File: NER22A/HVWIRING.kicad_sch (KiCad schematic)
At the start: 1 part

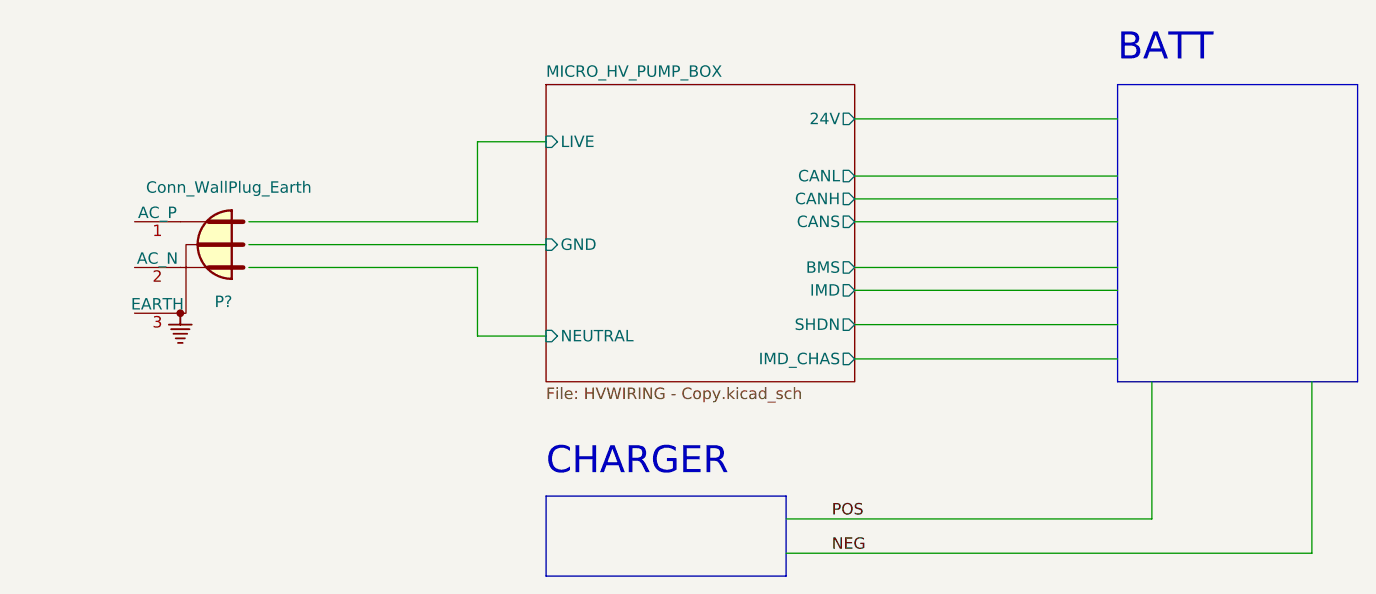
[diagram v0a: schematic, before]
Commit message: Finished wiring diagram
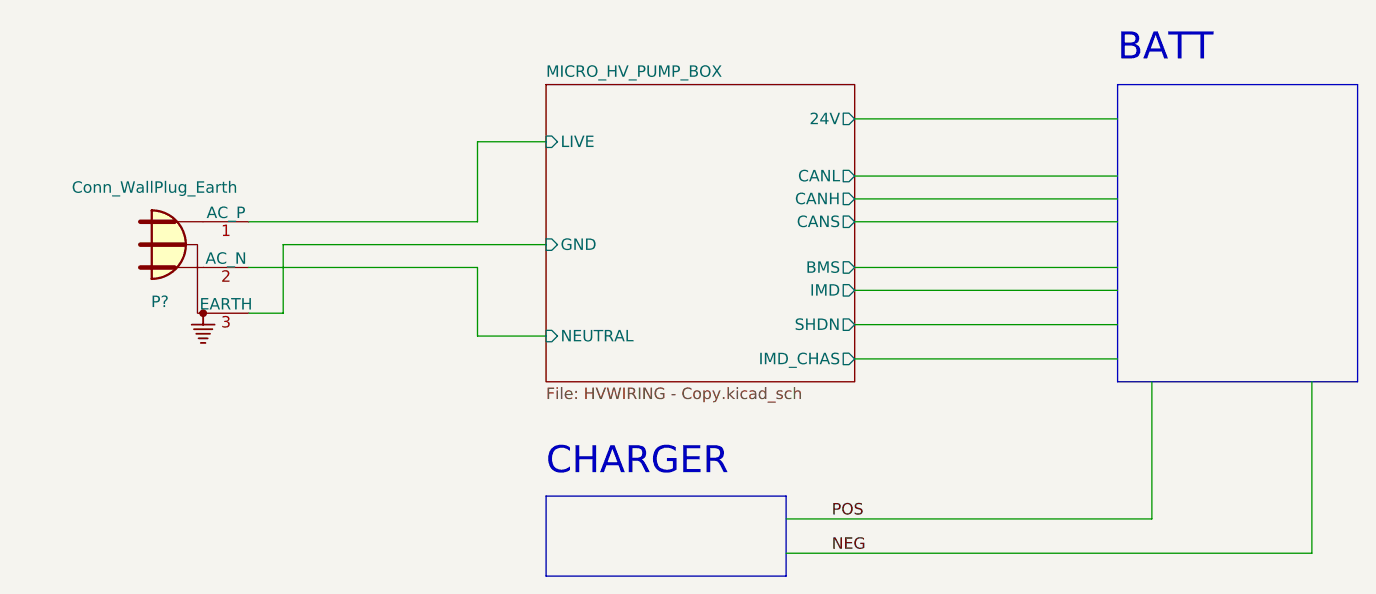
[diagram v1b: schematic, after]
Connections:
- net MICRO_HV_PUMP_BOX/GND: now also P?.3 (EARTH)
- net MICRO_HV_PUMP_BOX/LIVE: now also P?.1 (AC_P)
- net MICRO_HV_PUMP_BOX/NEUTRAL: now also P?.2 (AC_N)
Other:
- moved on the sheet: P?
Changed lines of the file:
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@@
 (kicad_sch (version 20230121) (generator eeschema)
-  (paper "A4")
+  (paper "A")
   (wire (pts (xy 157.48 88.9) (xy 157.48 104.14))
+    (stroke (width 0) (type default))
+  )
+  (wire (pts (xy 57.15 71.12) (xy 82.55 71.12))
     (stroke (width 0) (type default))
   )
@@
     (stroke (width 0) (type default))
   )
+  (wire (pts (xy 60.96 81.28) (xy 57.15 81.28))
+    (stroke (width 0) (type default))
+  )
   (polyline (pts (xy 90.17 101.6) (xy 116.84 101.6))
+    (stroke (width 0) (type default))
+  )
+  (wire (pts (xy 57.15 76.2) (xy 82.55 76.2))
     (stroke (width 0) (type default))
   )
@@
     (stroke (width 0) (type default))
   )
-  (polyline (pts (xy 90.17 101.6) (xy 90.17 110.49))
+  (wire (pts (xy 60.96 73.66) (xy 90.17 73.66))
     (stroke (width 0) (type default))
   )
-  (wire (pts (xy 57.15 73.66) (xy 90.17 73.66))
+  (polyline (pts (xy 90.17 101.6) (xy 90.17 110.49))
     (stroke (width 0) (type default))
   )
@@
     (stroke (width 0) (type default))
   )
-  (wire (pts (xy 116.84 104.14) (xy 157.48 104.14))
+  (wire (pts (xy 60.96 73.66) (xy 60.96 81.28))
     (stroke (width 0) (type default))
   )
-  (wire (pts (xy 57.15 76.2) (xy 82.55 76.2))
+  (wire (pts (xy 116.84 104.14) (xy 157.48 104.14))
     (stroke (width 0) (type default))
   )
@@
   )
   (wire (pts (xy 124.46 82.55) (xy 153.67 82.55))
-    (stroke (width 0) (type default))
-  )
-  (wire (pts (xy 57.15 71.12) (xy 82.55 71.12))
     (stroke (width 0) (type default))
   )
@@
     (effects (font (size 1.27 1.27)) (justify left bottom))
   )
-  (symbol (lib_id "Connector:Conn_WallPlug_Earth") (at 52.07 73.66 0) (mirror y) (unit 1)
+  (symbol (lib_id "Connector:Conn_WallPlug_Earth") (at 49.53 73.66 0) (unit 1)
     (in_bom yes) (on_board yes) (dnp no)
-    (property "Reference" "P?" (at 53.34 80.01 0)
+    (property "Reference" "P?" (at 48.26 80.01 0)
       (effects (font (size 1.27 1.27)) (justify right))
     )
-    (property "Value" "Conn_WallPlug_Earth" (at 45.72 67.31 0)
+    (property "Value" "Conn_WallPlug_Earth" (at 55.88 67.31 0)
       (effects (font (size 1.27 1.27)) (justify right))
     )
-    (property "Footprint" "" (at 41.91 73.66 0)
+    (property "Footprint" "" (at 59.69 73.66 0)
       (effects (font (size 1.27 1.27)) hide)
     )
-    (property "Datasheet" "~" (at 41.91 73.66 0)
+    (property "Datasheet" "~" (at 59.69 73.66 0)
       (effects (font (size 1.27 1.27)) hide)
     )
